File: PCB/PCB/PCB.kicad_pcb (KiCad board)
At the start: 2 copper layers, 79 x 38.5 mm, 7 parts, among them SW1 SW_Push, SW2 SW_Push, SW3 SW_Push, SW4 SW_Push, SW5 RotaryEncoder, U1 MOUDLE-SEEEDUINO-XIAO, U2 ER_OLEDM0.91_1x-I2C

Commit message: delete innecesary files and add new production files
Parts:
- SW5: value RotaryEncoder -> RotaryEncoder_Switch; footprint Rotary_Encoder:RotaryEncoder_Alps_EC11E_Vertical_H20mm -> Rotary_Encoder:RotaryEncoder_Alps_EC11E-Switch_Vertical_H20mm
- moved SW5 1.33 mm to (188.2, 71.5)
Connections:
- SW1 pad 1: Net-(U1-PB09_A7_D7_RX) -> GND
- SW5 pad A: Net-(U1-3V3) -> Net-(U1-PA4_A1_D1)
- SW5 pad B: GND -> Net-(U1-PA10_A2_D2)
- SW5 pad C: Net-(U1-PA4_A1_D1) -> GND
- U1 pad 3: unconnected-(U1-PA10_A2_D2-Pad3) -> Net-(U1-PA10_A2_D2)
- U1 pad 4: unconnected-(U1-PA11_A3_D3-Pad4) -> Net-(U1-PA11_A3_D3)
- U1 pad 8: Net-(U1-PB09_A7_D7_RX) -> GND
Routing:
- net Net-(U1-PA10_A2_D2): track 0.00 -> 107.0 mm
- net Net-(U1-PA4_A1_D1): track 0.00 -> 86.6 mm
- net GND: track 122.2 -> 189.8 mm
- net Net-(U1-PA11_A3_D3): track 0.00 -> 51.5 mm
- net Net-(U1-PB09_A7_D7_RX): track 41.5 -> 0.00 mm

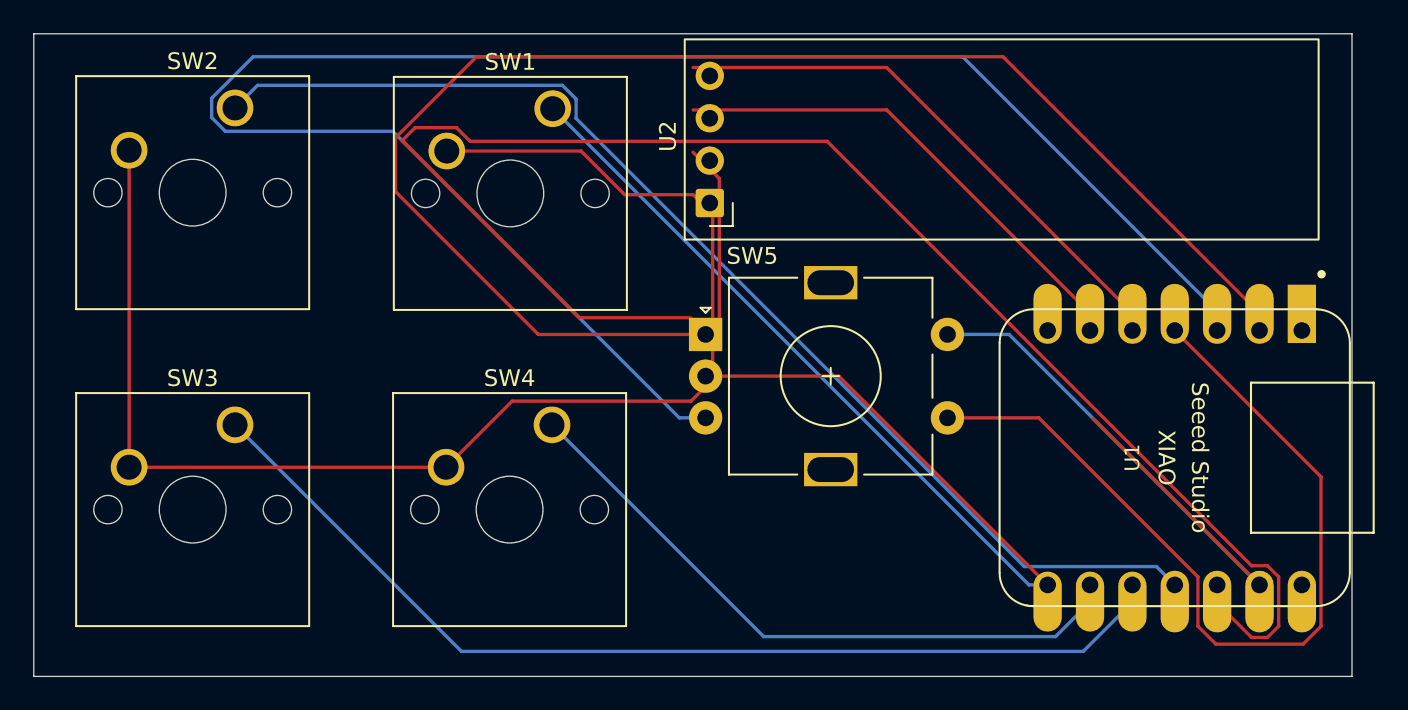
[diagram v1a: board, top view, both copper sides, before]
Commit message: Update PCB adding resistors
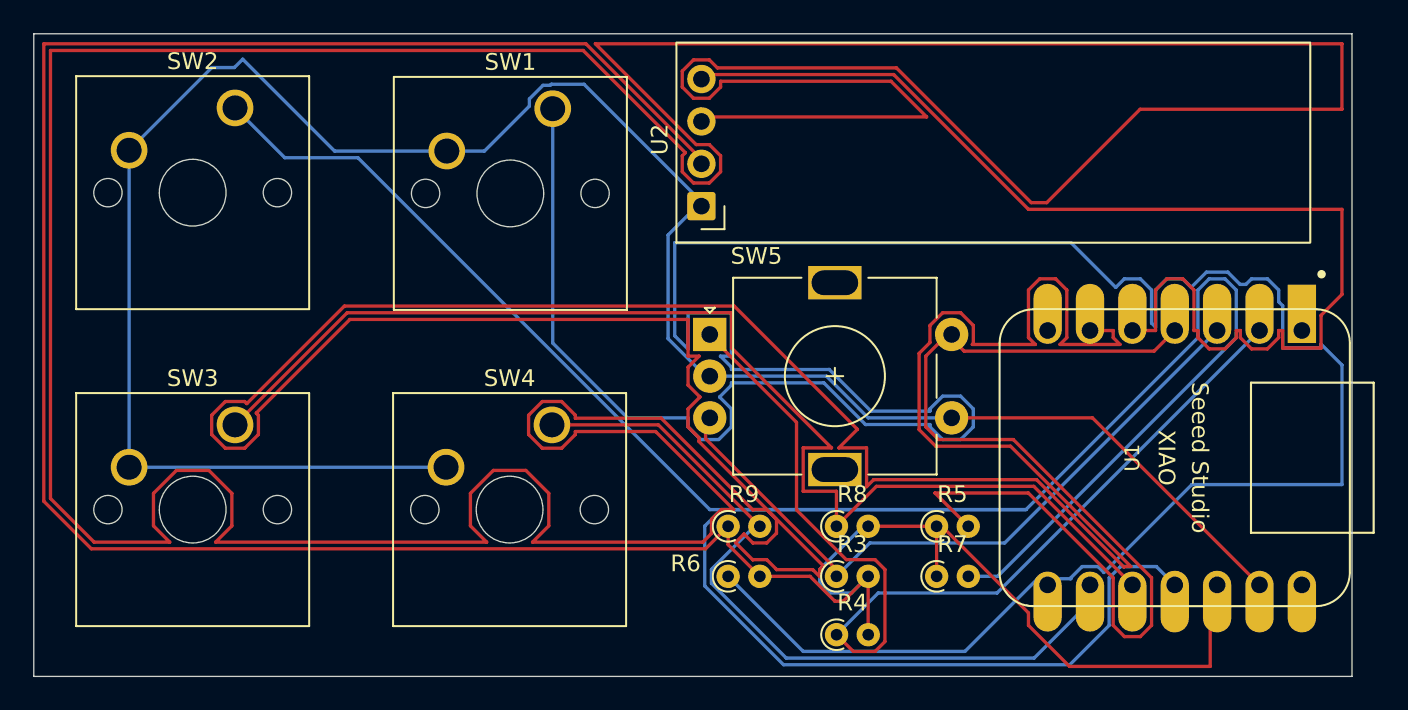
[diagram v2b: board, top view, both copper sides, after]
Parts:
- added R3: 4.7 k, Resistor_THT:R_Axial_DIN0204_L3.6mm_D1.6mm_P1.90mm_Vertical, F.Cu at (196.1, 86.0)
- added R4: 4.7 k, Resistor_THT:R_Axial_DIN0204_L3.6mm_D1.6mm_P1.90mm_Vertical, F.Cu at (196.1, 89.5)
- added R5: 4.7 k, Resistor_THT:R_Axial_DIN0204_L3.6mm_D1.6mm_P1.90mm_Vertical, F.Cu at (202.1, 83.0)
- added R6: 4.7 k, Resistor_THT:R_Axial_DIN0204_L3.6mm_D1.6mm_P1.90mm_Vertical, F.Cu at (189.6, 86.0)
- added R7: 4.7 k, Resistor_THT:R_Axial_DIN0204_L3.6mm_D1.6mm_P1.90mm_Vertical, F.Cu at (202.1, 86.0)
- added R8: 4.7 k, Resistor_THT:R_Axial_DIN0204_L3.6mm_D1.6mm_P1.90mm_Vertical, F.Cu at (196.1, 83.0)
- added R9: 4.7 k, Resistor_THT:R_Axial_DIN0204_L3.6mm_D1.6mm_P1.90mm_Vertical, F.Cu at (189.6, 83.0)
- moved U2 0.53 mm to (188.0, 63.8)
- moved SW5 0.25 mm to (188.5, 71.5)
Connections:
- SW1 pad 1: GND -> Net-(U1-PB09_A7_D7_RX)
- SW5 pad S1: Net-(U1-PA11_A3_D3) -> GND
- SW5 pad S2: GND -> Net-(U1-PA11_A3_D3)
- U1 pad 8: GND -> Net-(U1-PB09_A7_D7_RX)
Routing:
- net Net-(U1-PA9_A5_D5_SCL): track 29.9 -> 484.7 mm
- net Net-(U1-PB09_A7_D7_RX): track 0.00 -> 183.2 mm
- net Net-(U1-PA6_A10_D10_MOSI): track 70.0 -> 160.5 mm
- net Net-(U1-PA10_A2_D2): track 107.0 -> 41.7 mm
- net Net-(U1-3V3): track 105.2 -> 169.0 mm
- net GND: track 189.8 -> 132.3 mm
- net Net-(U1-PA8_A4_D4_SDA): track 33.5 -> 71.2 mm
- net Net-(U1-PA4_A1_D1): track 86.6 -> 60.2 mm
- net Net-(U1-PA5_A9_D9_MISO): track 61.7 -> 72.7 mm
- net Net-(U1-PA11_A3_D3): track 51.5 -> 62.1 mm
- net Net-(U1-PA7_A8_D8_SCK): track 39.4 -> 46.8 mm

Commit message: Add files via upload
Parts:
- removed R3, R4, R5, R6, R7, R8, R9: 4.7 k, Resistor_THT:R_Axial_DIN0204_L3.6mm_D1.6mm_P1.90mm_Vertical
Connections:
- SW5 pad A: Net-(U1-PA4_A1_D1) -> Net-(U1-PA02_A0_D0)
- SW5 pad B: Net-(U1-PA10_A2_D2) -> Net-(U1-PA11_A3_D3)
- SW5 pad S1: GND -> Net-(U1-PA10_A2_D2)
- SW5 pad S2: Net-(U1-PA11_A3_D3) -> Net-(U1-PA4_A1_D1)
- U1 pad 1: unconnected-(U1-PA02_A0_D0-Pad1) -> Net-(U1-PA02_A0_D0)
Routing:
- net Net-(U1-PA9_A5_D5_SCL): track 484.7 -> 29.3 mm
- net Net-(U1-PB09_A7_D7_RX): track 183.2 -> 45.1 mm
- net Net-(U1-3V3): track 169.0 -> 55.2 mm
- net Net-(U1-PA6_A10_D10_MOSI): track 160.5 -> 80.1 mm
- net Net-(U1-PA4_A1_D1): track 60.2 -> 0.00 mm
- net Net-(U1-PA02_A0_D0): track 0.00 -> 38.8 mm
- net Net-(U1-PA8_A4_D4_SDA): track 71.2 -> 32.7 mm
- net Net-(U1-PA11_A3_D3): track 62.1 -> 30.0 mm
- net Net-(U1-PA10_A2_D2): track 41.7 -> 18.1 mm
- net Net-(U1-PA5_A9_D9_MISO): track 72.7 -> 57.8 mm
- net GND: track 132.3 -> 125.9 mm
- net Net-(U1-PA7_A8_D8_SCK): track 46.8 -> 48.7 mm
